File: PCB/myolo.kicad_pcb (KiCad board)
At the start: 2 copper layers, 108 x 122 mm, 66 parts, among them J1 SiPM1 Connector, J2 SiPM2 Connector, J3 Conn_01x03_Socket, J4 Conn_01x03_Socket, U1 LM6172, U2 LM6172, U3 YAAJ_BluePill

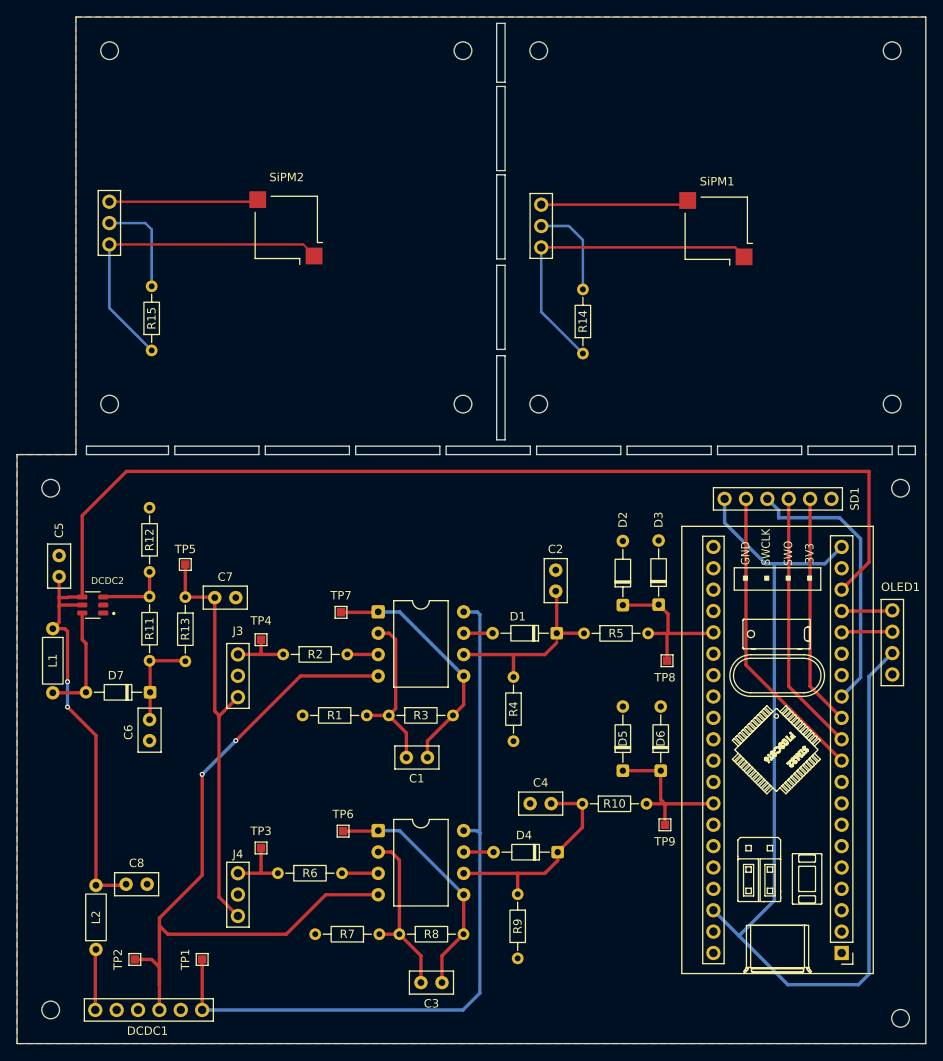
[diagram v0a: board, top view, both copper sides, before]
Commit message: added bom
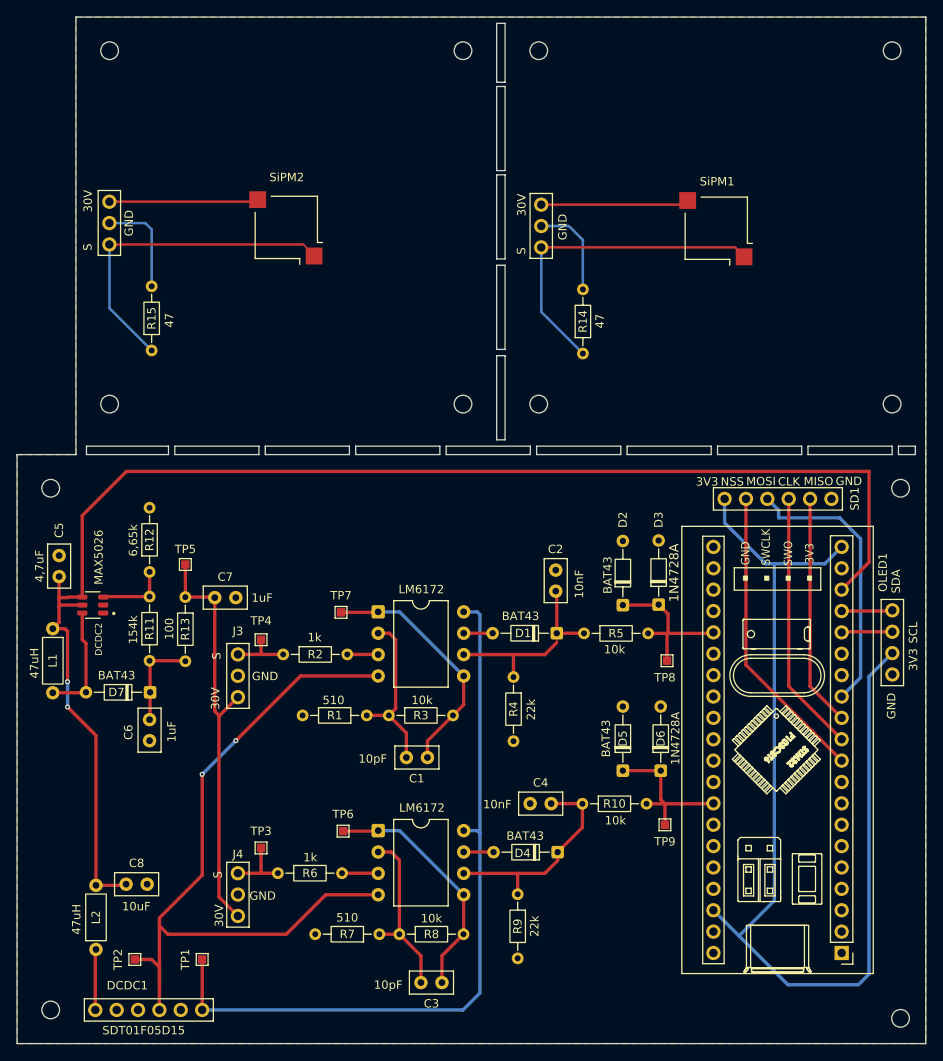
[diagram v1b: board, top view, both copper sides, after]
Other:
- board text added: "100"
- board text added: "10k"
- board text added: "10nF"
- board text added: "10pF"
- board text added: "10uF"
- board text added: "154k"
- board text added: "1N4728A"
- board text added: "1k"
- board text added: "1uF"
- board text added: "22k"
- board text added: "30V"
- board text added: "3V3"
- board text added: "4,7uF"
- board text added: "47"
- board text added: "47uH"
- board text added: "510"
- board text added: "6,65k"
- board text added: "BAT43"
- board text added: "CLK"
- board text added: "GND"
- board text added: "LM6172"
- board text added: "MAX5026"
- board text added: "MISO"
- board text added: "MOSI"
- board text added: "NSS"
- board text added: "S"
- board text added: "SCL"
- board text added: "SDA"
- board text added: "SDT01F05D15"

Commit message: added GND test point to pcb
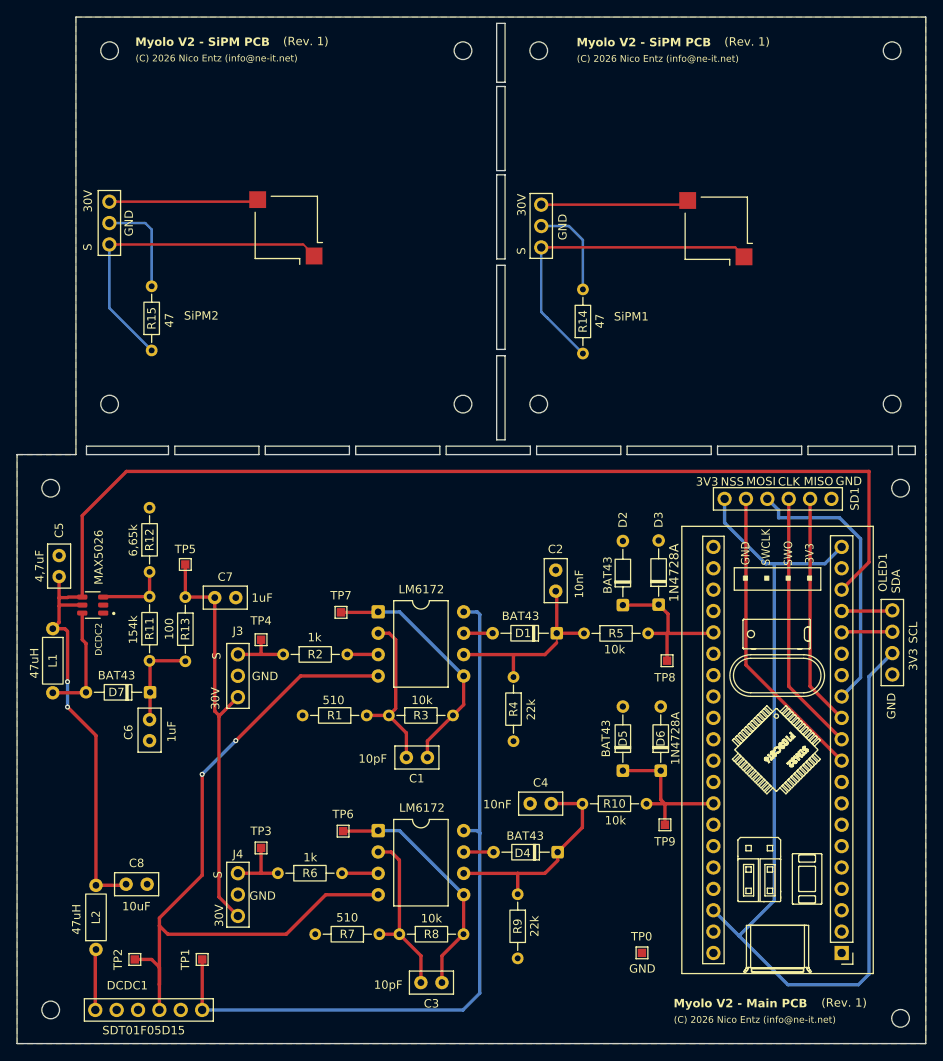
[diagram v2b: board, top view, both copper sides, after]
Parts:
- added TP0: TestPoint, TestPoint:TestPoint_Pad_1.0x1.0mm, F.Cu at (132.3, 162.2)
- R14, R15: value 50 -> 47
- R4, R9: value 20k -> 22k
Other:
- board text added: "(C) 2026 Nico Entz (info@ne-it.net)"
- board text added: "(Rev. 1)"
- board text added: "Myolo V2 - Main PCB"
- board text added: "Myolo V2 - SiPM PCB"

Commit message: added debug oscilloscope screenshots
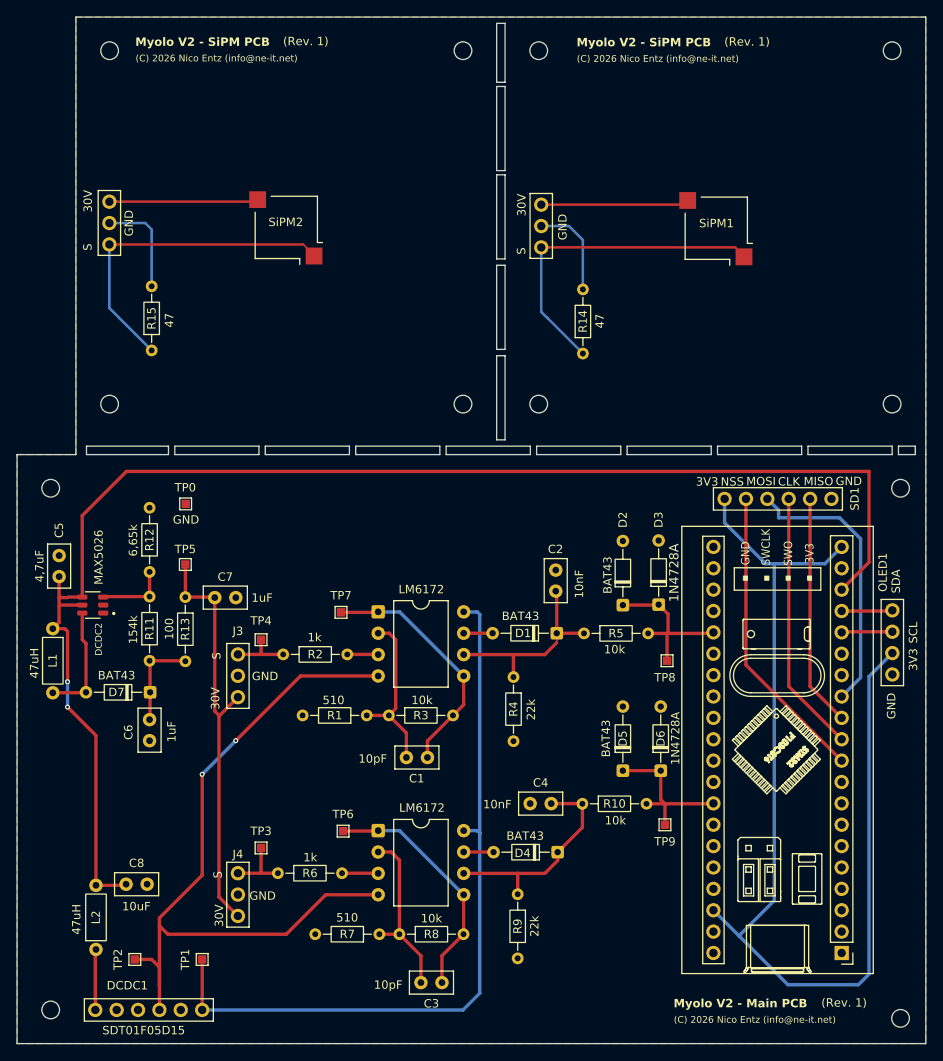
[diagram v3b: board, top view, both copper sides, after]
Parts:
- moved TP0 76.1 mm to (78.0, 108.9)
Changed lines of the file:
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@@
 	(footprint "TestPoint:TestPoint_Pad_1.0x1.0mm"
 		(layer "F.Cu")
-		(at 132.27 162.22)
+		(at 78.04 108.86)
 		(descr "SMD rectangular pad as test Point, square 1.0mm side length")
 		(tags "test point SMD pad rectangle square")
@@
 		(at 79.9 87)
 		(property "Reference" "SiPM2"
-			(at 0 -0.5 0)
+			(at 10.04 -11.62 0)
 			(unlocked yes)
 			(layer "F.SilkS")
@@
 		)
 		(property "Value" "MicroFC-60035-SMT"
-			(at 0 1 0)
+			(at 11.36 -4.56 0)
 			(unlocked yes)
 			(layer "F.Fab")
@@
 		)
 		(fp_text user "${REFERENCE}"
-			(at 0 2.5 0)
+			(at 11.36 -3.06 0)
 			(unlocked yes)
 			(layer "F.Fab")
@@
 		(at 131 87.1)
 		(property "Reference" "SiPM1"
-			(at 0 -0.5 0)
+			(at 10.12 -11.58 0)
 			(unlocked yes)
 			(layer "F.SilkS")
@@
 		)
 		(property "Value" "MicroFC-60035-SMT"
-			(at 0 1 0)
+			(at 9.68 -3.49 0)
 			(unlocked yes)
 			(layer "F.Fab")
@@
 		)
 		(fp_text user "${REFERENCE}"
-			(at 0 2.5 0)
+			(at 9.68 -1.99 0)
 			(unlocked yes)
 			(layer "F.Fab")
@@
 	)
 	(gr_text "GND"
-		(at 130.74 164.69 0)
+		(at 76.51 111.33 0)
 		(layer "F.SilkS")
 		(effects

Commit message: updated pcb
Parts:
- SD1: footprint Custom:1x6 NoGND -> Custom:SdHEAD
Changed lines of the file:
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@@
 		)
 	)
-	(footprint "Custom:1x6 NoGND"
+	(footprint "Custom:SdHEAD"
 		(layer "F.Cu")
 		(at 154.79 108.26274 -90)
-		(descr "Through hole straight socket strip, 1x06, 2.54mm pitch, single row (from Kicad 4.0.7), script generated")
-		(tags "Through hole socket strip THT 1x06 2.54mm single row")
+		(descr "Through hole straight pin header, 1x06, 2.54mm pitch, single row")
+		(tags "Through hole pin header THT 1x06 2.54mm single row")
 		(property "Reference" "SD1"
-			(at 0 -2.77 270)
+			(at 0 -2.38 270)
 			(layer "F.SilkS")
 			(effects
@@
 		)
 		(property "Value" "SDBrOut"
-			(at 0 15.47 270)
+			(at 0 15.08 270)
 			(layer "F.Fab")
-			(hide yes)
 			(effects
 				(font
@@
 		(attr through_hole)
 		(fp_line
-			(start -1.33 14.03)
-			(end 1.33 14.03)
+			(start -1.38 14.08)
+			(end 1.38 14.08)
 			(stroke
 				(width 0.12)
@@
 		)
 		(fp_line
-			(start -1.33 -1.3)
-			(end -1.33 14.03)
+			(start -1.38 -1.3)
+			(end -1.38 14.08)
 			(stroke
 				(width 0.12)
@@
 		)
 		(fp_line
-			(start -1.33 -1.3)
-			(end 1.33 -1.3)
+			(start -1.38 -1.3)
+			(end 1.38 -1.3)
 			(stroke
 				(width 0.12)
@@
 		)
 		(fp_line
-			(start 1.33 -1.3)
-			(end 1.33 14.03)
+			(start 1.38 -1.3)
+			(end 1.38 14.08)
 			(stroke
 				(width 0.12)
@@
 			(layer "F.SilkS")
 		)
-		(fp_line
-			(start -1.8 14.45)
-			(end -1.8 -1.8)
+		(fp_rect
+			(start -1.77 -1.77)
+			(end 1.77 14.47)
 			(stroke
 				(width 0.05)
 				(type solid)
 			)
+			(fill no)
 			(layer "F.CrtYd")
 		)
 		(fp_line
-			(start 1.75 14.45)
-			(end -1.8 14.45)
+			(start -1.27 13.97)
+			(end -1.3 -1.3)
 			(stroke
-				(width 0.05)
+				(width 0.1)
 				(type solid)
 			)
-			(layer "F.CrtYd")
+			(layer "F.Fab")
 		)
 		(fp_line
-			(start -1.8 -1.8)
-			(end 1.75 -1.8)
+			(start 1.27 13.97)
+			(end -1.27 13.97)
 			(stroke
-				(width 0.05)
+				(width 0.1)
 				(type solid)
 			)
-			(layer "F.CrtYd")
+			(layer "F.Fab")
 		)
 		(fp_line
-			(start 1.75 -1.8)
-			(end 1.75 14.45)
+			(start 1.27 -1.27)
+			(end 1.27 13.97)
 			(stroke
-				(width 0.05)
+				(width 0.1)
 				(type solid)
 			)
-			(layer "F.CrtYd")
+			(layer "F.Fab")
 		)
 		(fp_line
-			(start 1.27 13.97)
-			(end -1.27 13.97)
+			(start -1.3 -1.3)
+			(end 1.27 -1.27)
 			(stroke
 				(width 0.1)
@@
 		)
 		(embedded_fonts no)
-		(model "${KICAD9_3DMODEL_DIR}/Connector_PinSocket_2.54mm.3dshapes/PinSocket_1x06_P2.54mm_Vertical.step"
+		(model "${KICAD9_3DMODEL_DIR}/Connector_PinHeader_2.54mm.3dshapes/PinHeader_1x06_P2.54mm_Vertical.step"
 			(offset
 				(xyz 0 0 0)
@@
 			(layer "F.Fab")
 		)
+		(fp_text user "${REFERENCE}"
+			(at 0 6.35 180)
+			(layer "F.Fab")
+			(effects
+				(font
+					(size 1 1)
+					(thickness 0.15)
+				)
+			)
+		)
 		(pad "1" thru_hole circle
 			(at 0 0 90)
@@
 			(pintype "input")
 		)
-		(pad "3" thru_hole circle
-			(at 0 5.08 90)
-			(size 1.7 1.7)
-			(drill 1)
-			(layers "*.Cu" "*.Mask")
-			(remove_unused_layers no)
-		)
 		(pad "4" thru_hole circle
 			(at 0 7.62 90)
@@
 	)
 	(gr_text "Myolo V2 - SiPM PCB"
-		(at 72.05 54.55 0)
+		(at 72.81 54.47 0)
 		(layer "F.SilkS")
 		(effects
@@
 	)
 	(gr_text "(C) 2026 Nico Entz (info@ne-it.net)"
-		(at 72.08 56.37 0)
+		(at 72.71 56.3 0)
 		(layer "F.SilkS")
 		(effects
@@
 	)
 	(gr_text "(Rev. 1)"
-		(at 89.61 54.47 0)
+		(at 90.38 54.36 0)
 		(layer "F.SilkS")
 		(effects
